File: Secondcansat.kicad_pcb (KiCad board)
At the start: 2 copper layers, 92.5 x 86.5 mm, 61 parts, among them IC1 XBP9B-XCWT-001, J1 OpenlogBreakout, J10 SDA, J11 5V, J12 Tx, J13 Rx, J14 Battery_Holder_keystone 1079, J15 USB_B_Mini, J16 coinBattery, J2 Camera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

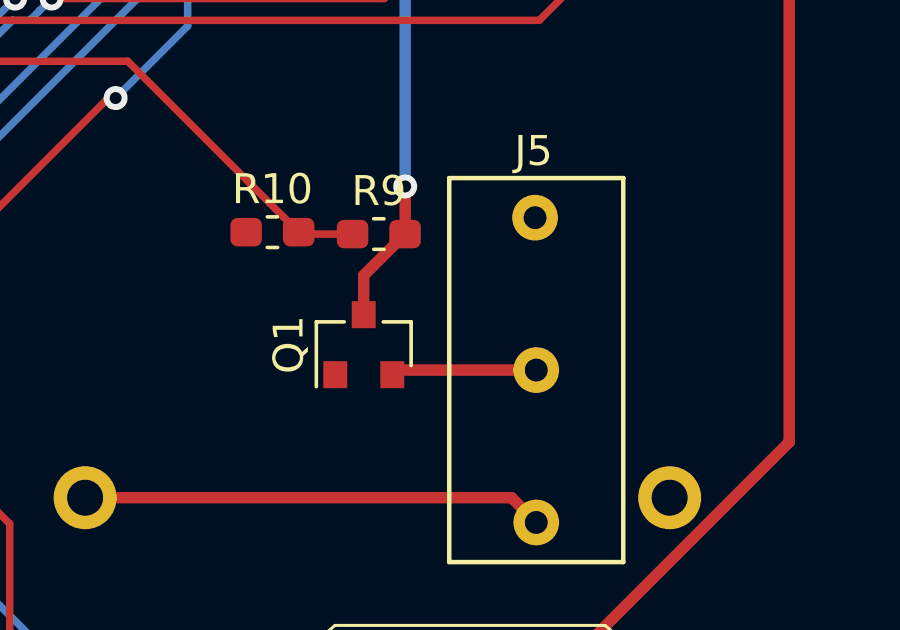
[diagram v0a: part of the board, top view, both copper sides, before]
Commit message: reversed source and drain in the Pchannel mosfet
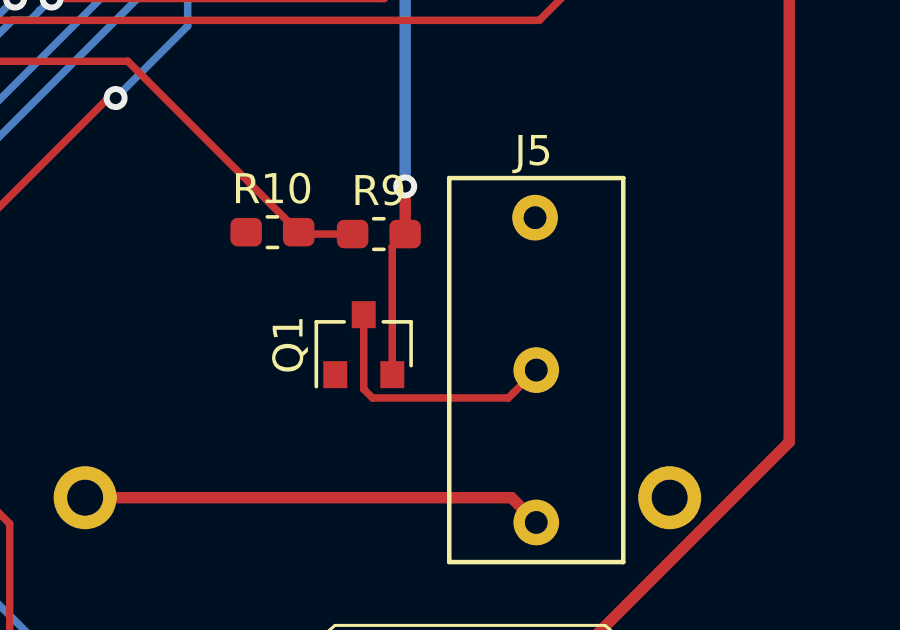
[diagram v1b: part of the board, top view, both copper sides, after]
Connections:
- Q1 pad 1: +6V -> Net-(J5-Pad2)
- Q1 pad 3: Net-(J5-Pad2) -> +6V
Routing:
- net Net-(J5-Pad2): track 4.86 -> 8.74 mm
- net +6V: track 104.9 -> 106.7 mm
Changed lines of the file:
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@@
     (thickness 1.6)
     (drawings 6)
-    (tracks 569)
+    (tracks 573)
     (zones 0)
     (modules 61)
@@
   )
   (setup
-    (last_trace_width 0.381)
+    (last_trace_width 0.25)
     (user_trace_width 0.381)
     (trace_clearance 0.2)
@@
       (net 3 GND))
     (pad 3 smd rect (at -1 0.95 90) (size 0.9 0.8) (layers F.Cu F.Paste F.Mask)
-      (net 43 "Net-(J5-Pad2)"))
-    (pad 1 smd rect (at 1 0 90) (size 0.9 0.8) (layers F.Cu F.Paste F.Mask)
       (net 2 +6V))
+    (pad 1 smd rect (at 1 0 90) (size 0.9 0.8) (layers F.Cu F.Paste F.Mask)
+      (net 43 "Net-(J5-Pad2)"))
     (model ${KISYS3DMOD}/Package_TO_SOT_SMD.3dshapes/SOT-23.wrl
       (at (xyz 0 0 0))
@@
   (segment (start 81.8007 34.1319) (end 95.2684 47.5996) (width 0.381) (layer F.Cu) (net 2))
   (segment (start 81.8007 31.0436) (end 81.8007 34.1319) (width 0.381) (layer F.Cu) (net 2))
-  (segment (start 147.9194 58.6435) (end 149.2986 57.2643) (width 0.381) (layer F.Cu) (net 2))
-  (segment (start 147.9194 59.9506) (end 147.9194 58.6435) (width 0.381) (layer F.Cu) (net 2))
   (via (at 113.6396 43.0276) (size 0.8) (drill 0.4) (layers F.Cu B.Cu) (net 2))
   (segment (start 95.2684 47.5996) (end 99.8404 43.0276) (width 0.381) (layer B.Cu) (net 2))
@@
   (segment (start 152.8442 66.0524) (end 153.67 66.8782) (width 0.381) (layer F.Cu) (net 42))
   (segment (start 138.6322 66.0524) (end 152.8442 66.0524) (width 0.381) (layer F.Cu) (net 42))
-  (segment (start 149.0218 61.7982) (end 148.8694 61.9506) (width 0.381) (layer F.Cu) (net 43))
-  (segment (start 153.67 61.7982) (end 149.0218 61.7982) (width 0.381) (layer F.Cu) (net 43))
+  (segment (start 149.0218 61.7982) (end 148.8694 61.9506) (width 0.381) (layer F.Cu) (net 2))
+  (segment (start 148.8694 57.6935) (end 149.2986 57.2643) (width 0.25) (layer F.Cu) (net 2))
+  (segment (start 148.8694 61.9506) (end 148.8694 57.6935) (width 0.25) (layer F.Cu) (net 2))
+  (segment (start 152.908001 62.560199) (end 153.67 61.7982) (width 0.25) (layer F.Cu) (net 43))
+  (segment (start 152.742599 62.725601) (end 152.908001 62.560199) (width 0.25) (layer F.Cu) (net 43))
+  (segment (start 148.209399 62.725601) (end 152.742599 62.725601) (width 0.25) (layer F.Cu) (net 43))
+  (segment (start 147.9194 62.435602) (end 148.209399 62.725601) (width 0.25) (layer F.Cu) (net 43))
+  (segment (start 147.9194 59.9506) (end 147.9194 62.435602) (width 0.25) (layer F.Cu) (net 43))
   (segment (start 106.74908 67.69912) (end 106.68 67.63004) (width 0.25) (layer F.Cu) (net 44))
   (segment (start 106.74908 69.82968) (end 106.74908 67.69912) (width 0.25) (layer F.Cu) (net 44))
